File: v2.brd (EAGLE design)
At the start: 24 x 24 mm, 42 parts, among them Q1 12MHz

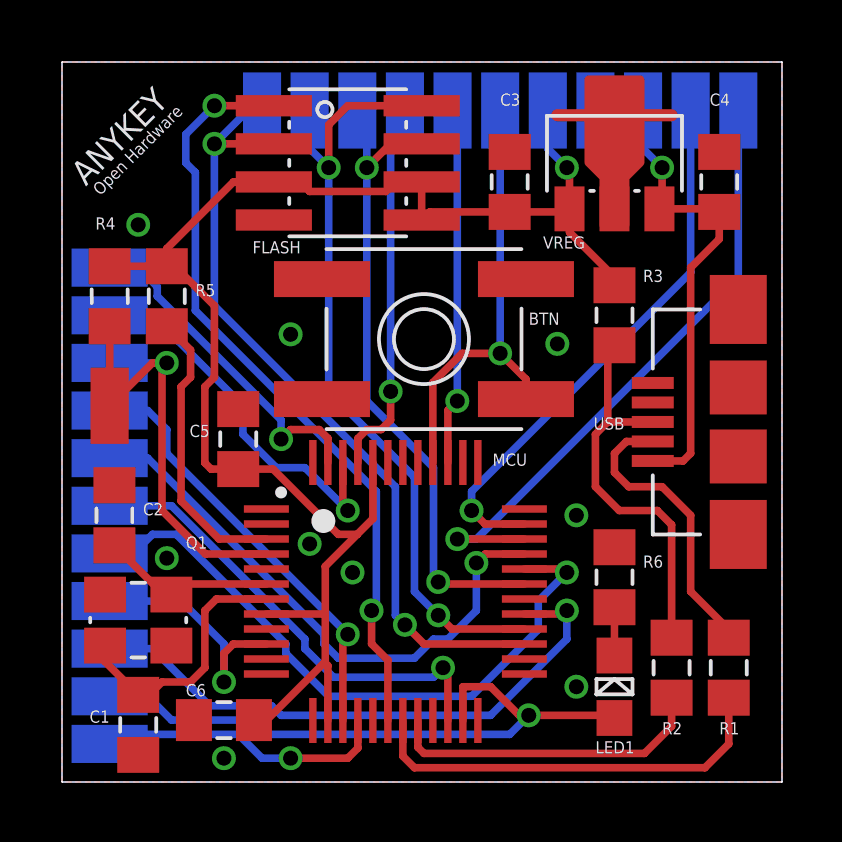
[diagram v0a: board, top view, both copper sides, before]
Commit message: changed voltage regulator, routed more pins
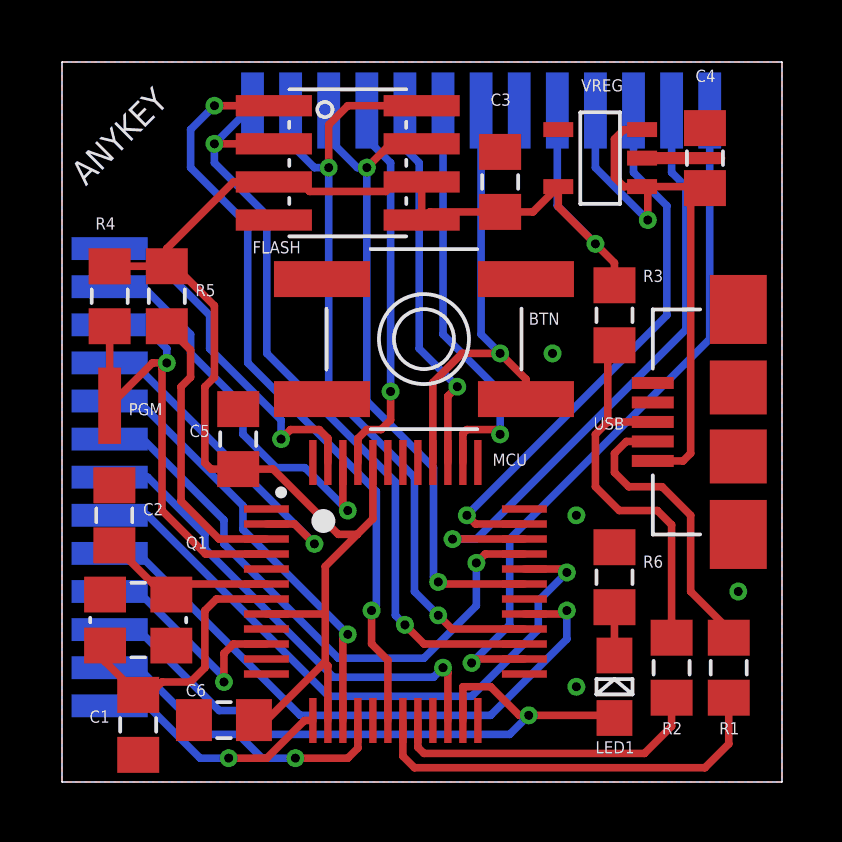
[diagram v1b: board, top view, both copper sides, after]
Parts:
- added JP23: PIO2_0, MEINZEUG:PCB_MEDIUM_RECT_PAD
- added JP24: PIO2_1, MEINZEUG:PCB_MEDIUM_RECT_PAD
- added JP25: PIO2_2, MEINZEUG:PCB_MEDIUM_RECT_PAD
- added JP26: PIO2_3, MEINZEUG:PCB_MEDIUM_RECT_PAD
- VREG: device MEINZEUG:SOT89-3 -> MEINZEUG:SOT-23-5
- moved JP10 3.17 mm to (1.59, 7.62), turned to 180 degrees
- moved JP22 2.54 mm to (15.2, 22.4)
- moved JP4 2.54 mm to (1.59, 3.81), turned to 180 degrees
- moved JP13 2.22 mm to (20.3, 22.4)
- moved JP6 2.22 mm to (1.59, 5.08), turned to 180 degrees
- moved JP14 1.90 mm to (19.1, 22.4)
- moved JP15 1.59 mm to (11.4, 22.4)
- moved JP21 1.59 mm to (17.8, 22.4)
- moved JP11 1.27 mm to (1.59, 8.89), turned to 180 degrees
- moved JP1 1.27 mm to (1.59, 15.2), turned to 180 degrees
- moved JP17 1.27 mm to (10.2, 22.4)
- moved JP18 0.95 mm to (1.59, 16.5), turned to 180 degrees
- moved JP5 0.95 mm to (1.59, 10.2), turned to 180 degrees
- moved JP9 0.95 mm to (8.89, 22.4)
- moved C4 0.93 mm to (21.4, 20.8)
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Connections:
- new net PIO2_0: JP23.P$1, MCU.2
- new net PIO2_1: JP24.P$1, MCU.13
- new net PIO2_2: JP25.P$1, MCU.26
- new net PIO2_3: JP26.P$1, MCU.38
- net VD33: now also VREG.5; no longer VREG.1
- net VPOWER: now also VREG.1
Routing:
- net PIO2_2: track 0.00 -> 23.5 mm, vias 0 -> 1
- net PIO2_3: track 0.00 -> 13.9 mm, vias 0 -> 1
- net PIO2_0: track 0.00 -> 11.2 mm, vias 0 -> 1
- net PIO2_1: track 0.00 -> 8.02 mm, vias 0 -> 1
- net VPOWER: track 15.5 -> 21.5 mm
- net VD33: track 53.3 -> 55.6 mm
- net PIO0_10: track 19.6 -> 20.9 mm
- net GND: track 3.81 -> 2.57 mm, vias 9 -> 4
- net PIO0_7: track 21.4 -> 22.3 mm
- net PIO0_5: track 9.79 -> 10.6 mm
- net PIO1_6: track 12.9 -> 13.6 mm
- net PIO1_7: track 11.3 -> 12.0 mm
- net SCK: track 21.9 -> 22.5 mm
- net PIO0_1: track 16.3 -> 16.9 mm
- net PIO1_3: track 12.0 -> 12.6 mm
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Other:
- board text removed: "Open Hardware"

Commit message: vreg label 1801
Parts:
- VREG: value MCP1804 -> MCP1801
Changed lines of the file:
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@@
 Covered vias can be set in Masks (Limit).
 &lt;/p&gt;Your Beta LAYOUT Team</description>
+<description language="en">&lt;b&gt;EAGLE Design Rules&lt;/b&gt;
+&lt;p&gt;
+The default Design Rules have been set to cover
+a wide range of applications. Your particular design
+may have different requirements, so please make the
+necessary adjustments and save your customized
+design rules under a new name.
+</description>
 <param name="layerSetup" value="(1*16)"/>
 <param name="mtCopper" value="0.035mm 0.035mm 0.035mm 0.035mm 0.035mm 0.035mm 0.035mm 0.035mm 0.035mm 0.035mm 0.035mm 0.035mm 0.035mm 0.035mm 0.035mm 0.035mm"/>
@@
 <attribute name="VALUE" x="14.351" y="9.9695" size="0.4064" layer="27" font="vector"/>
 </element>
-<element name="VREG" library="MEINZEUG" package="SOT-23-5" value="MCP1804" x="17.93875" y="20.79625" smashed="yes" rot="R90">
+<element name="VREG" library="MEINZEUG" package="SOT-23-5" value="MCP1801" x="17.93875" y="20.79625" smashed="yes" rot="R90">
 <attribute name="NAME" x="17.30375" y="23.01875" size="0.4064" layer="25" font="vector"/>
 <attribute name="VALUE" x="16.8275" y="22.38375" size="0.4064" layer="27" font="vector"/>
